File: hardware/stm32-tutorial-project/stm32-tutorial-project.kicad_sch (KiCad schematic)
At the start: 24 parts, among them SW1 SW_Push, SW2 SW_Push_SPDT, U1 STM32G431CBTx

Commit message: added programming header
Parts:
- added J2: 10pin IDC SWD, Connector_IDC:IDC-Header_2x05_P2.54mm_Vertical, symbol Connector_Generic:Conn_02x05_Odd_Even
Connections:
- net +3.3V: now also J2.7 (Pin_7), J2.8 (Pin_8)
- net GND: now also J2.3 (Pin_3), J2.4 (Pin_4)
- net NRST: now also J2.1 (Pin_1)
- net SW_CLK: now reaches U1.37 (PA13)
- net SW_DIO: now reaches U1.38 (PA14)
- net SWO: now reaches U1.40 (PB3)
- net SWO: now also J2.5 (Pin_5)
- new net +5V: J2.10 (Pin_10), J2.9 (Pin_9)
- new net SWCLK: J2.6 (Pin_6)
- new net SWDIO: J2.2 (Pin_2)
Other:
- note added: "SWD PROGRAMMING HEADER"

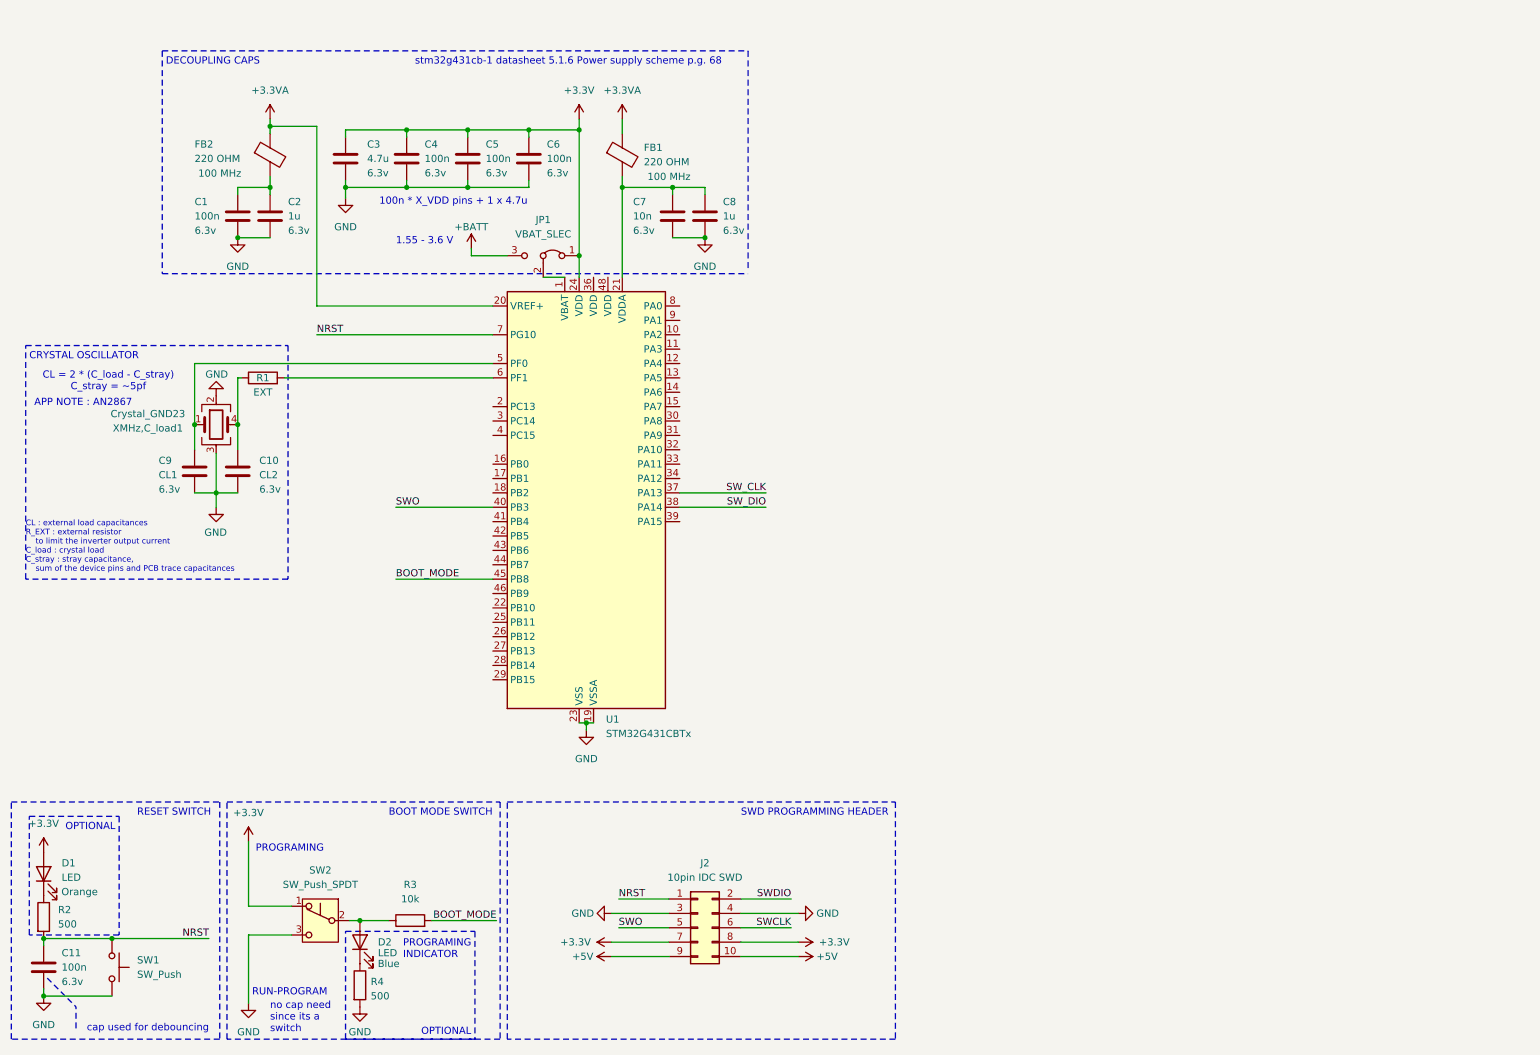
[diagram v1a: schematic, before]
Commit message: added usb port to pcb
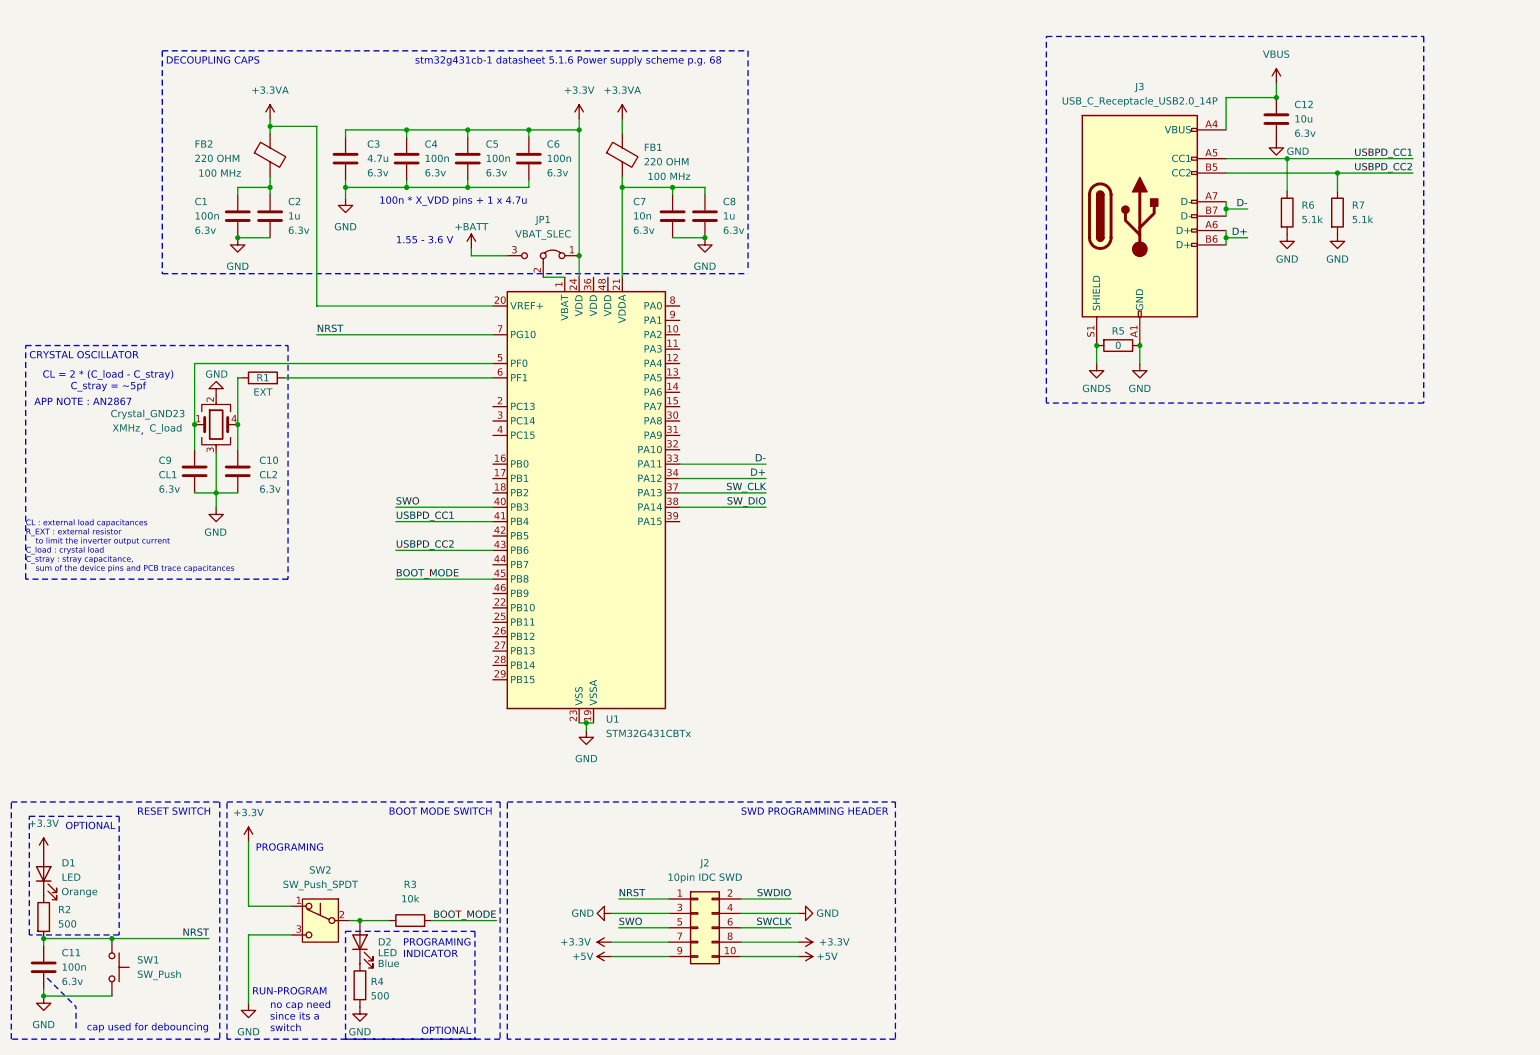
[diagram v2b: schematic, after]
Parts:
- added C12: 10u, symbol Device:C
- added J3: USB_C_Receptacle_USB2.0_14P, symbol Connector:USB_C_Receptacle_USB2.0_14P
- added R5: 0, symbol Device:R
- added R6, R7: 5.1k, symbol Device:R
- XMHz: renamed from XMHz,C_load1; LoadCapacitance (none) -> C_load
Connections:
- net GND: now also C12.2, J3.A1 (GND), J3.A12 (GND), J3.B1 (GND), J3.B12 (GND), R5.1, R6.2, R7.2
- net D-: now reaches U1.33 (PA11)
- net D-: now also J3.A7 (D-), J3.B7 (D-)
- net D+: now reaches U1.34 (PA12)
- net D+: now also J3.A6 (D+), J3.B6 (D+)
- net USBPD_CC1: now reaches U1.41 (PB4)
- net USBPD_CC1: now also J3.A5 (CC1), R6.1
- net USBPD_CC2: now reaches U1.43 (PB6)
- net USBPD_CC2: now also J3.B5 (CC2), R7.1
- new net GNDS: J3.S1 (SHIELD), R5.2
- new net VBUS: C12.1, J3.A4 (VBUS), J3.A9 (VBUS), J3.B4 (VBUS), J3.B9 (VBUS)
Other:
- note added: ","

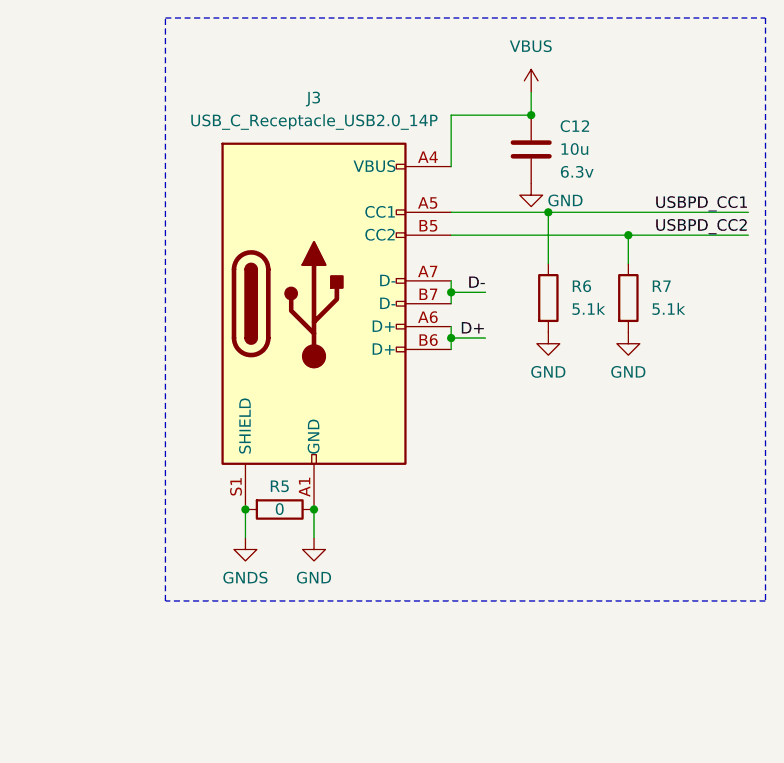
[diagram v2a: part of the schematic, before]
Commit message: moved usb c into hierarchically sheet
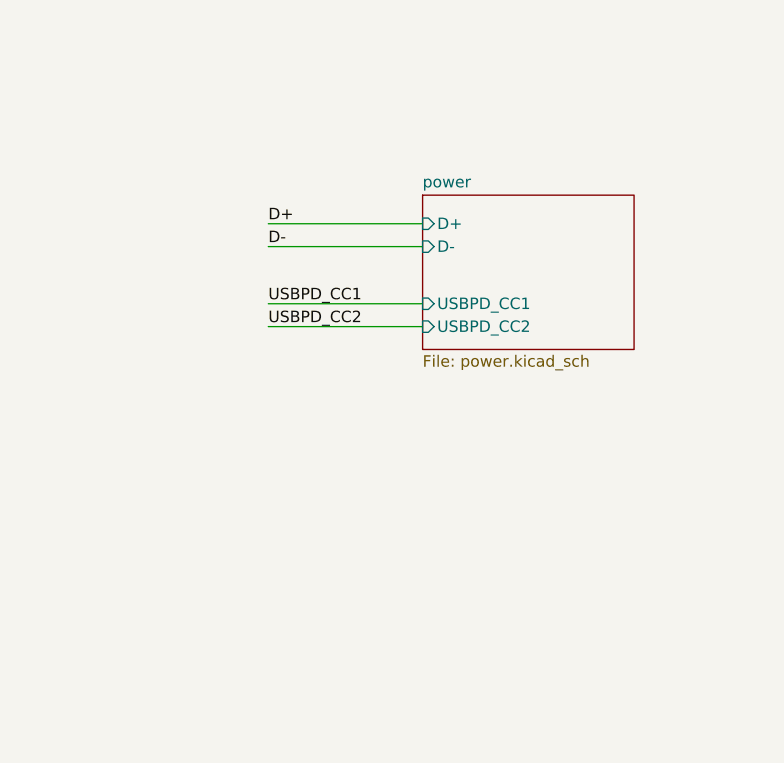
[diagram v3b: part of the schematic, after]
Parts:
- removed C12: 10u, symbol Device:C
- removed J3: USB_C_Receptacle_USB2.0_14P, symbol Connector:USB_C_Receptacle_USB2.0_14P
- removed R5: 0, symbol Device:R
- removed R6, R7: 5.1k, symbol Device:R
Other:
- added sheet power (power.kicad_sch)

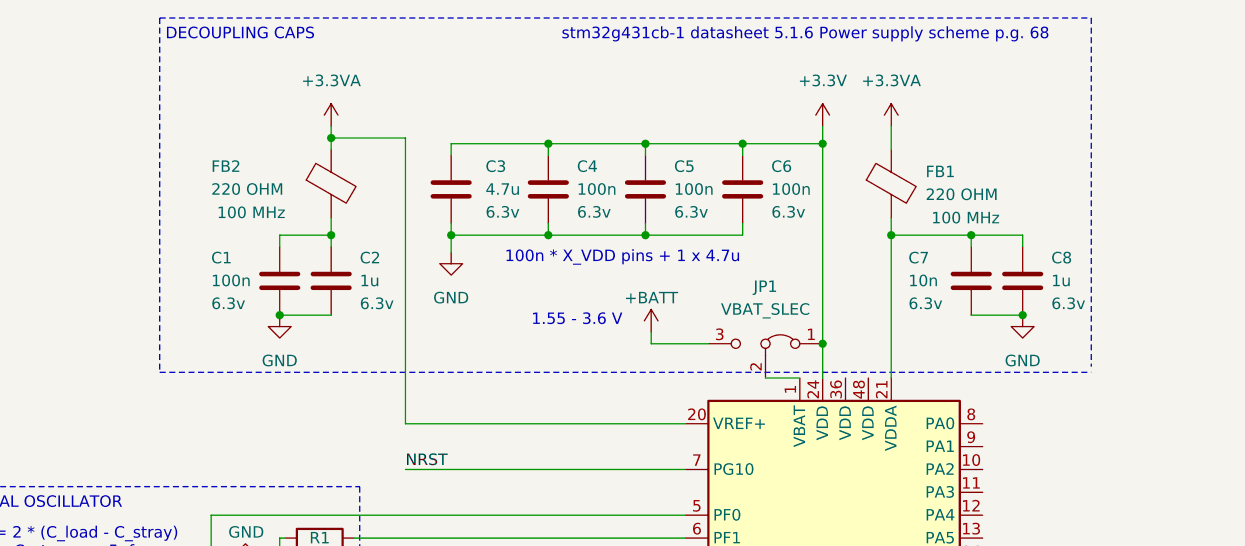
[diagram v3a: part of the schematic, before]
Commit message: updated power circuit with more info on or-ing circuit voltags and added status leds
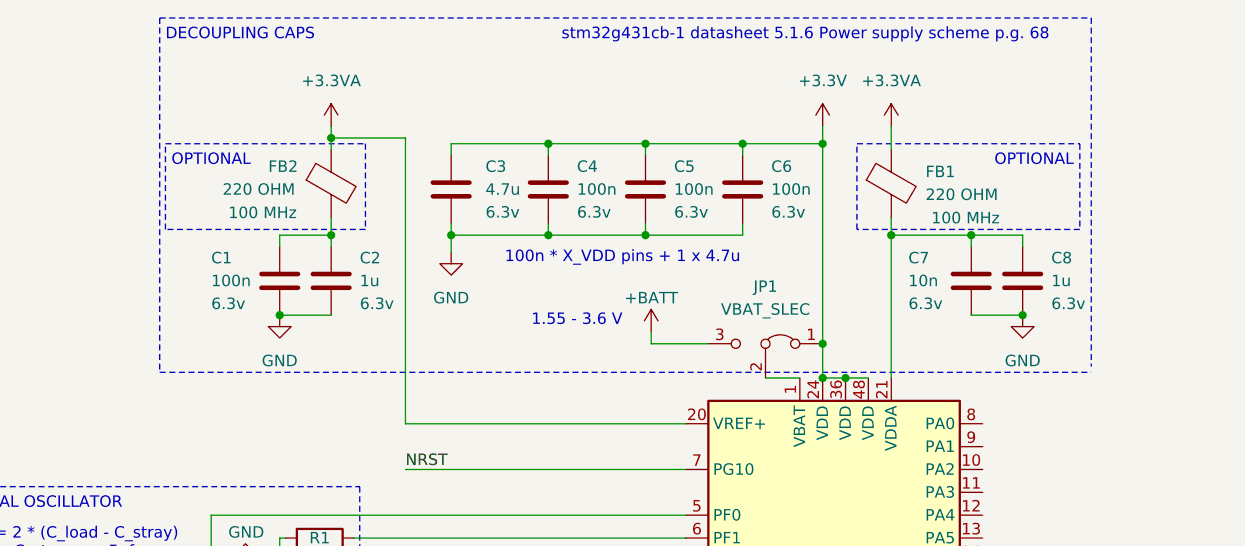
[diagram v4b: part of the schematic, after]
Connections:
- net +3.3V: now also U1.36 (VDD), U1.48 (VDD)
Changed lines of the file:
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@@
 	)
 	(junction
+		(at 114.3 60.96)
+		(diameter 0)
+		(color 0 0 0 0)
+	)
+	(junction
 		(at 83.82 34.925)
 		(diameter 0)
@@
 	)
 	(junction
+		(at 116.84 60.96)
+		(diameter 0)
+		(color 0 0 0 0)
+	)
+	(junction
 		(at 19.685 177.8)
 		(diameter 0)
@@
 	(wire
 		(pts
+			(xy 116.84 60.96) (xy 119.38 60.96)
+		)
+		(stroke
+			(width 0)
+			(type default)
+		)
+	)
+	(wire
+		(pts
 			(xy 46.355 99.06) (xy 50.165 99.06)
 		)
@@
 	(wire
 		(pts
+			(xy 114.3 60.96) (xy 116.84 60.96)
+		)
+		(stroke
+			(width 0)
+			(type default)
+		)
+	)
+	(wire
+		(pts
 			(xy 59.69 35.56) (xy 59.69 34.29)
 		)
@@
 	)
 	(rectangle
+		(start 118.11 34.925)
+		(end 142.875 44.45)
+		(stroke
+			(width 0)
+			(type dot)
+		)
+		(fill
+			(type none)
+		)
+	)
+	(rectangle
+		(start 41.275 34.925)
+		(end 63.5 44.45)
+		(stroke
+			(width 0)
+			(type dot)
+		)
+		(fill
+			(type none)
+		)
+	)
+	(rectangle
 		(start 101.6 153.67)
 		(end 170.18 195.58)
@@
 		)
 	)
+	(text "OPTIONAL"
+		(exclude_from_sim no)
+		(at 137.795 36.83 0)
+		(effects
+			(font
+				(size 1.27 1.27)
+			)
+		)
+	)
 	(text "1.55 - 3.6 V"
 		(exclude_from_sim no)
@@
 		)
 	)
+	(text "OPTIONAL"
+		(exclude_from_sim no)
+		(at 46.355 36.83 0)
+		(effects
+			(font
+				(size 1.27 1.27)
+			)
+		)
+	)
 	(text "CL : external load capacitances\nR_EXT : external resistor \n	to limit the inverter output current\nC_load : crystal load\nC_stray : stray capacitance, \n	sum of the device pins and PCB trace capacitances"
 		(exclude_from_sim no)
@@
 		(dnp no)
 		(property "Reference" "FB2"
-			(at 46.355 37.465 0)
+			(at 52.705 37.465 0)
 			(effects
 				(font
@@
 		)
 		(property "Value" "220 OHM"
-			(at 46.355 40.005 0)
+			(at 47.625 40.005 0)
 			(effects
 				(font
@@
 		)
 		(property "Frequency" "100 MHz"
-			(at 50.8 42.5959 0)
+			(at 52.07 42.5959 0)
 			(effects
 				(font
